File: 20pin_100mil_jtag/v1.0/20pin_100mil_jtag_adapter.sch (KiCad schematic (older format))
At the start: 2 parts, among them X1 JTAG-10, X2 JTAG-20

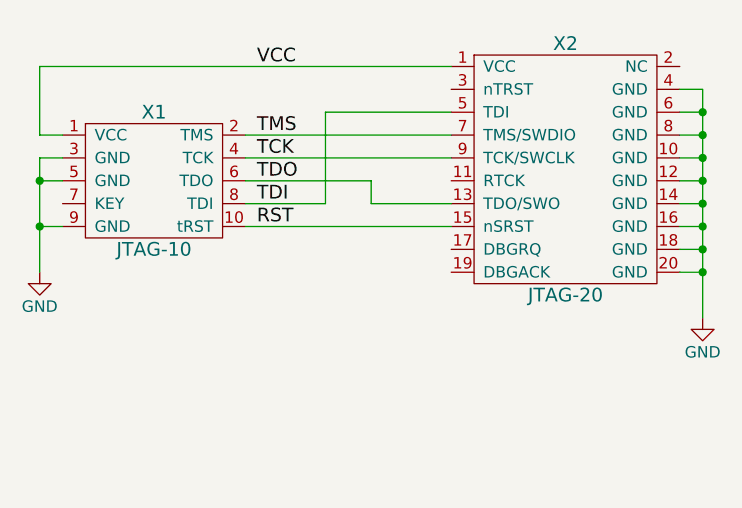
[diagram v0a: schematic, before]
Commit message: Added VCC jumper to the adapter.
The VCC jumper is connected by default, but it makes it possible to cut
the circuit open and then use a solder jumper to close it again. Some
added flexibility... :)
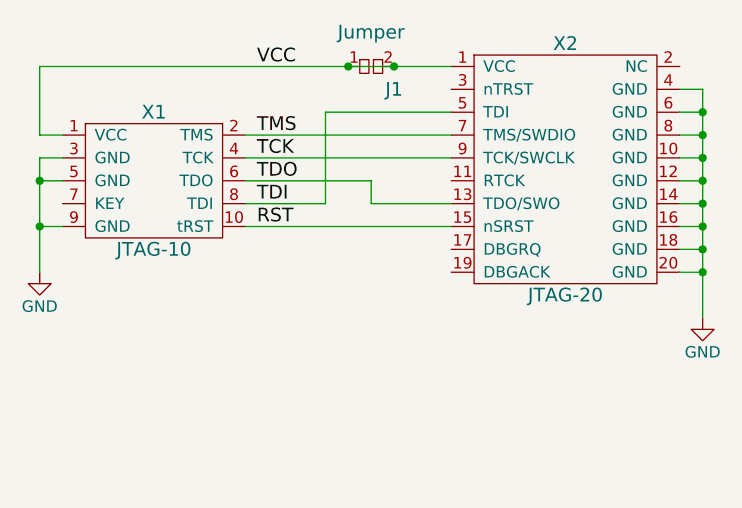
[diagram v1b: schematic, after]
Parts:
- added J1: Jumper, pkl_jumpers:J_0402, symbol Jumper
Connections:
- net VCC: now also J1.1, J1.2
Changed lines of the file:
@@
 LIBS:pkl_sensor
 LIBS:pkl_texas
+LIBS:20pin_100mil_jtag_adapter-cache
 EELAYER 25 0
 EELAYER END
@@
 Text Label 5200 2950 0    60   ~ 0
 VCC
+$Comp
+L Jumper J1
+U 1 1 56C38629
+P 5700 2950
+F 0 "J1" H 5800 2850 60  0000 C CNN
+F 1 "Jumper" H 5700 3100 60  0000 C CNN
+F 2 "pkl_jumpers:J_0402" H 5700 2950 60  0001 C CNN
+F 3 "" H 5700 2950 60  0000 C CNN
+F 4 "ANY" H 5700 2950 60  0001 C CNN "Source"
+	1    5700 2950
+	1    0    0    -1
+$EndComp
+Connection ~ 5800 2950
+Connection ~ 5600 2950
 $EndSCHEMATC

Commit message: Added reset button to the 20pin adapter.
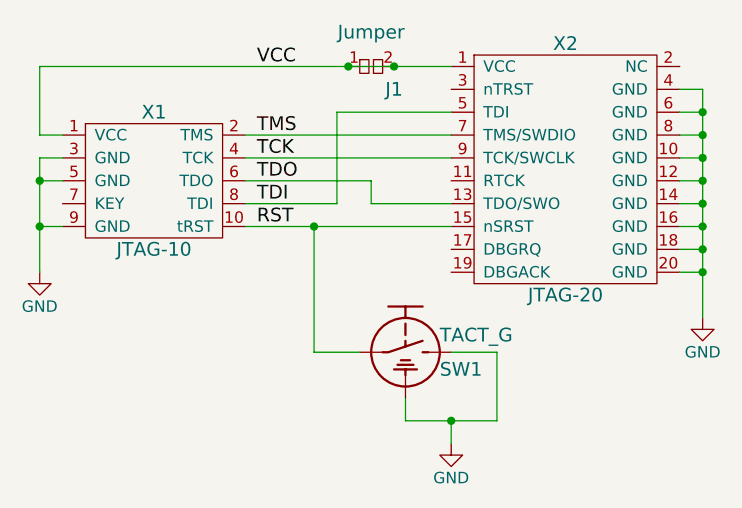
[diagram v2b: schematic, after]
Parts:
- added SW1: TACT_G, pkl_buttons_switches:Tact_Switch_Top_GND_B3U-1100P, symbol TACT_G
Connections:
- net GND: now also SW1.2, SW1.GND (case)
- net RST: now also SW1.1
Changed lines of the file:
@@
 	5700 3550 6050 3550
 Wire Wire Line
-	5150 3550 5500 3550
+	5150 3550 5550 3550
 Wire Wire Line
-	5500 3550 5500 3150
+	5550 3550 5550 3150
 Wire Wire Line
-	5500 3150 6050 3150
+	5550 3150 6050 3150
 Wire Wire Line
 	5150 3650 6050 3650
@@
 Connection ~ 7150 3850
 $Comp
-L GND #PWR2
+L GND #PWR01
 U 1 1 56B3A386
 P 7150 4050
-F 0 "#PWR2" H 7150 3800 50  0001 C CNN
+F 0 "#PWR01" H 7150 3800 50  0001 C CNN
 F 1 "GND" H 7150 3900 50  0000 C CNN
 F 2 "" H 7150 4050 50  0000 C CNN
@@
 $EndComp
 $Comp
-L GND #PWR1
+L GND #PWR02
 U 1 1 56B3A39E
 P 4250 3850
-F 0 "#PWR1" H 4250 3600 50  0001 C CNN
+F 0 "#PWR02" H 4250 3600 50  0001 C CNN
 F 1 "GND" H 4250 3700 50  0000 C CNN
 F 2 "" H 4250 3850 50  0000 C CNN
@@
 Connection ~ 5800 2950
 Connection ~ 5600 2950
+$Comp
+L TACT_G SW1
+U 1 1 56C4161E
+P 5850 4200
+F 0 "SW1" H 6000 4125 60  0000 L CNN
+F 1 "TACT_G" H 6000 4275 60  0000 L CNN
+F 2 "pkl_buttons_switches:Tact_Switch_Top_GND_B3U-1100P" H 5850 4175 60  0001 C CNN
+F 3 "" H 5850 4175 60  0000 C CNN
+F 4 "ANY" H 5850 4200 60  0001 C CNN "Source"
+	1    5850 4200
+	1    0    0    -1
+$EndComp
+Connection ~ 5450 3650
+Wire Wire Line
+	5450 4200 5650 4200
+Wire Wire Line
+	5450 3650 5450 4200
+Wire Wire Line
+	6050 4200 6250 4200
+Wire Wire Line
+	6250 4200 6250 4500
+Wire Wire Line
+	6250 4500 5850 4500
+Wire Wire Line
+	5850 4500 5850 4400
+$Comp
+L GND #PWR03
+U 1 1 56C418A0
+P 6050 4600
+F 0 "#PWR03" H 6050 4350 50  0001 C CNN
+F 1 "GND" H 6050 4450 50  0000 C CNN
+F 2 "" H 6050 4600 50  0000 C CNN
+F 3 "" H 6050 4600 50  0000 C CNN
+	1    6050 4600
+	1    0    0    -1
+$EndComp
+Wire Wire Line
+	6050 4500 6050 4600
+Connection ~ 6050 4500
 $EndSCHEMATC
